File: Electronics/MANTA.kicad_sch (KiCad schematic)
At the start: 36 parts, among them J1 LORA_UP, J2 LORA_DOWN

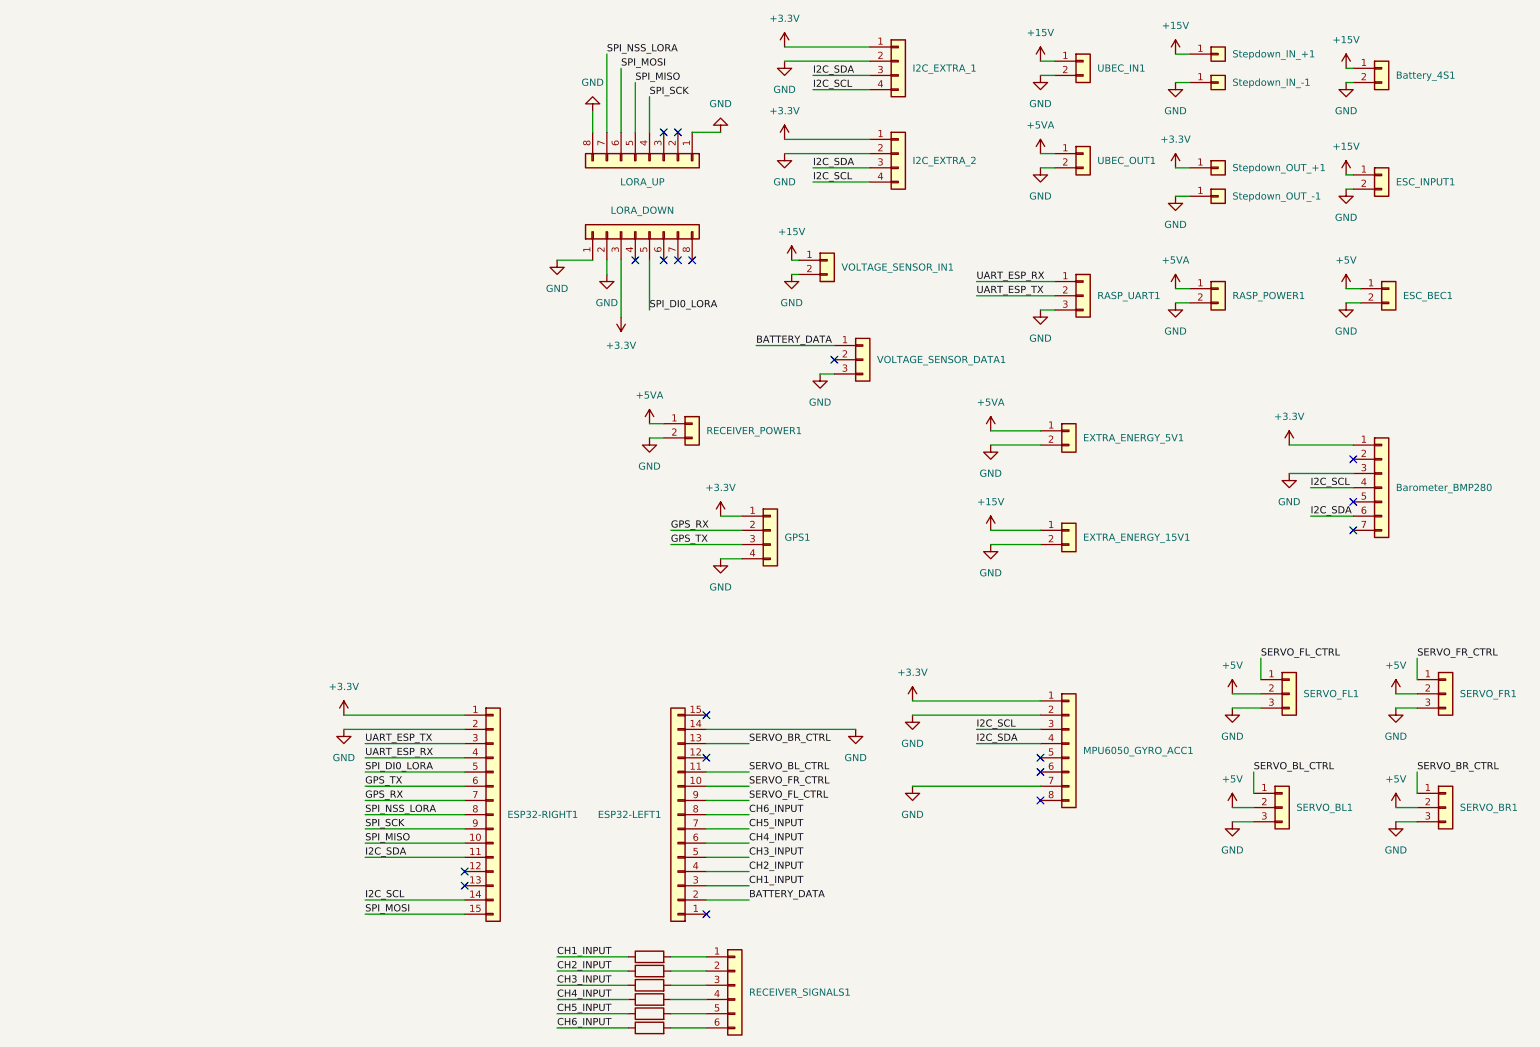
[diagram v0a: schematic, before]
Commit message: general fixes - todo: split into 2 boards <= 10mm
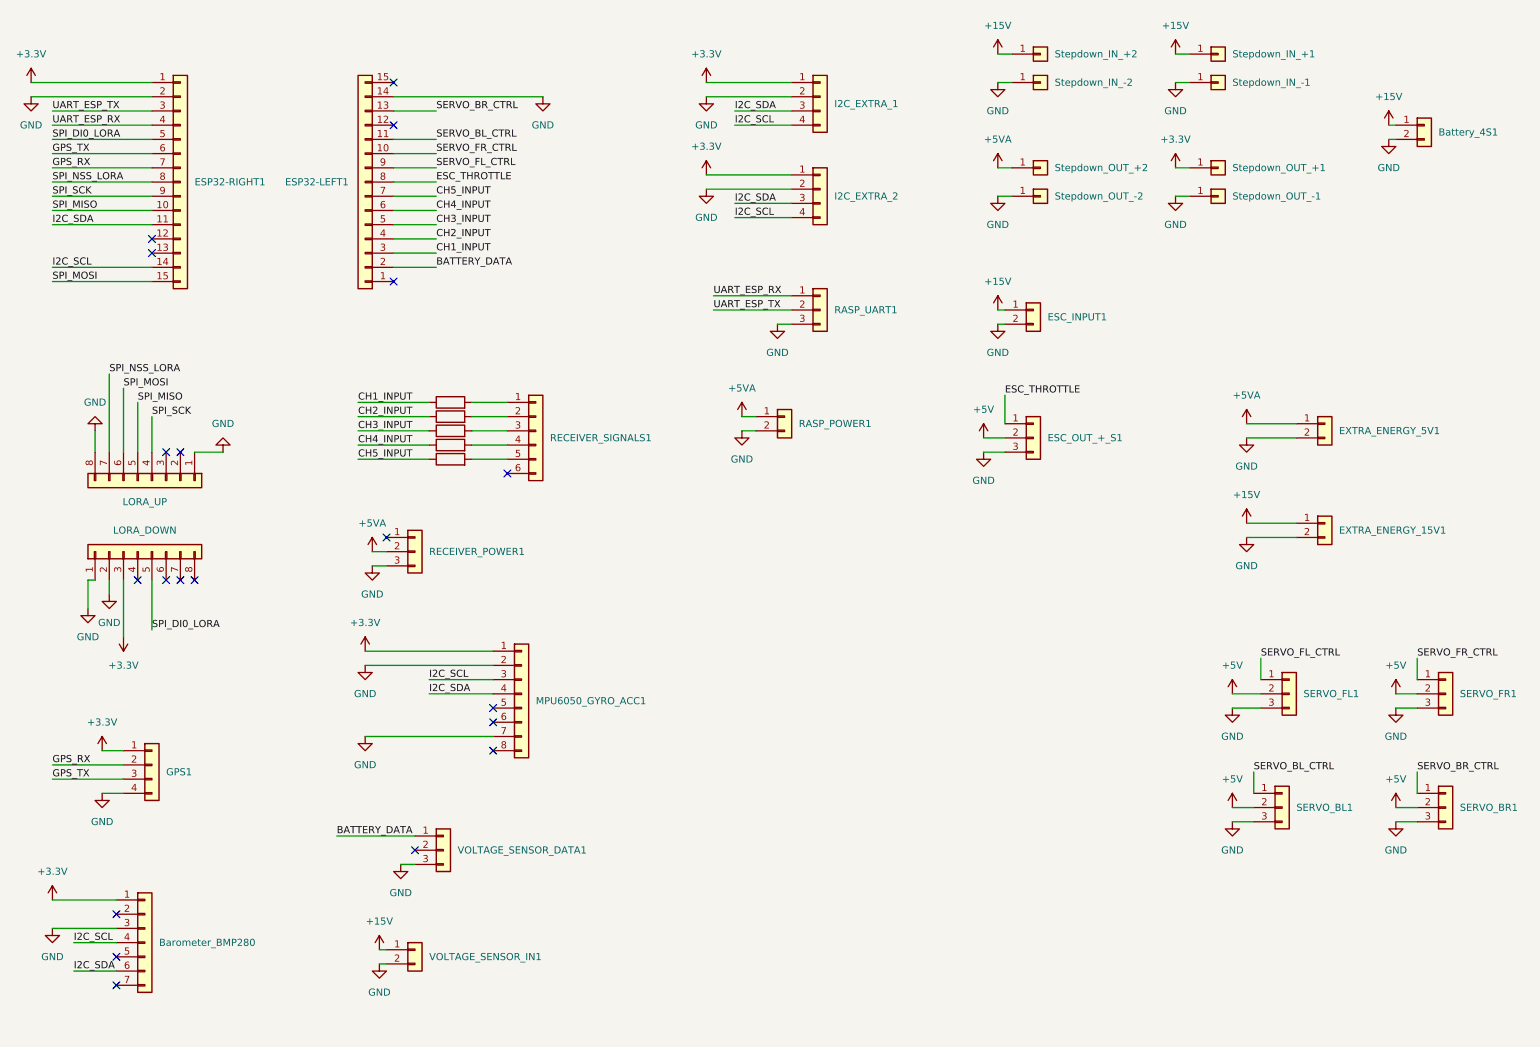
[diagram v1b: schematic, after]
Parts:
- removed ESC_BEC1, RECEIVER_POWER1, UBEC_IN1, UBEC_OUT1: Conn_01x02, Connector_PinHeader_2.54mm:PinHeader_1x02_P2.54mm_Vertical, symbol Connector_Generic:Conn_01x02
- removed R6: 1k, Resistor_THT:R_Axial_DIN0207_L6.3mm_D2.5mm_P10.16mm_Horizontal, symbol Device:R
- added ESC_OUT_+_S1, RECEIVER_POWER1: Conn_01x03, Connector_PinHeader_2.54mm:PinHeader_1x03_P2.54mm_Vertical, symbol Connector_Generic:Conn_01x03
- added Stepdown_IN_+2, Stepdown_IN_-2, Stepdown_OUT_+2, Stepdown_OUT_-2: Conn_01x01, Connector_PinHeader_2.54mm:PinHeader_1x01_P2.54mm_Vertical, symbol Connector_Generic:Conn_01x01
- Battery_4S1: footprint Connector_Wire:SolderWire-6sqmm_1x02_P14mm_D3.5mm_OD7mm -> Connector_AMASS:AMASS_XT60PW-M_1x02_P7.20mm_Horizontal
- ESC_INPUT1: footprint Connector_Wire:SolderWire-6sqmm_1x02_P14mm_D3.5mm_OD7mm -> Connector_Wire:SolderWire-2.5sqmm_1x02_P8.8mm_D2.4mm_OD4.4mm
- VOLTAGE_SENSOR_IN1: footprint Connector_Wire:SolderWire-6sqmm_1x02_P14mm_D3.5mm_OD7mm -> Connector_PinHeader_2.54mm:PinHeader_1x02_P2.54mm_Vertical
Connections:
- net +15V: now also Stepdown_IN_+2.1 (Pin_1)
- net +5V: now also ESC_OUT_+_S1.2 (Pin_2)
- net +5VA: now also RECEIVER_POWER1.2 (Pin_2), Stepdown_OUT_+2.1 (Pin_1)
- net GND: now also ESC_OUT_+_S1.3 (Pin_3), RECEIVER_POWER1.3 (Pin_3), Stepdown_IN_-2.1 (Pin_1), Stepdown_OUT_-2.1 (Pin_1)
- net CH6_INPUT renamed ESC_THROTTLE
- net ESC_THROTTLE: now also ESC_OUT_+_S1.1 (Pin_1)
- no-connect marks 18 -> 20
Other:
- company: (none) -> MANTA
- title: (none) -> MAIN PCB
- moved on the sheet: Barometer_BMP280, Battery_4S1, ESC_INPUT1, ESP32-LEFT1, ESP32-RIGHT1, EXTRA_ENERGY_15V1, EXTRA_ENERGY_5V1, GPS1, I2C_EXTRA_1, I2C_EXTRA_2, MPU6050_GYRO_ACC1, RASP_POWER1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
